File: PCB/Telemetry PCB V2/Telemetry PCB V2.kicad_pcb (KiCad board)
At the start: 4 copper layers, 47 parts, among them IC1 E22-900M22S, J1 USB_C_Receptacle_USB2.0_16P, J2 Batt, J3 Serial Debug Header 1x4, J4 GPS, J5 Conn_01x04_Pin, SW1 SW_MEC_5E, SW2 SW_MEC_5E, U1 AP62200WU, U2 STM32F411CEUx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

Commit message: Corrected spi and uart connections
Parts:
- added C1: 0.1uF, Capacitor_SMD:C_1206_3216Metric_Pad1.33x1.80mm_HandSolder, F.Cu at (208.6, 82.1)
- added D3: WS2812B, LED_SMD:LED_WS2812B_PLCC4_5.0x5.0mm_P3.2mm, F.Cu at (209.6, 77.1)
- C12: value 2.2uF -> 4.7uF
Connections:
- IC1 pad 15: NRST -> TRST
- J4 pad 1: +5V -> +3.3V
- U2 pad 25: RX2 -> TX2
- U2 pad 26: TX2 -> RX2
- U2 pad 29: RX -> unconnected-(U2-PA8-Pad29)
- U2 pad 31: SWDIO -> RX
- U2 pad 32: SWCLK -> unconnected-(U2-PA11-Pad32)
- U2 pad 33: RXEN -> unconnected-(U2-PA12-Pad33)
- U2 pad 34: TXEN -> SWDIO
- U2 pad 37: NSS -> SWCLK
- U2 pad 38: SCK -> unconnected-(U2-PA15-Pad38)
- U2 pad 39: MOSI -> SCK
- U2 pad 41: unconnected-(U2-PB5-Pad41) -> MOSI
- U2 pad 42: BUSY -> unconnected-(U2-PB6-Pad42)
- U2 pad 43: DIO1 -> unconnected-(U2-PB7-Pad43)
- U2 pad 9: VREF+ -> +3.3V
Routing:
- net RXEN: track 44.7 -> 0.00 mm
- net TXEN: track 44.3 -> 0.00 mm
- net BOOT0: track 20.2 -> 0.00 mm
- net SWDIO: track 18.7 -> 0.00 mm
- net SWCLK: track 16.0 -> 0.00 mm
- net DIO1: track 14.9 -> 0.00 mm
- net NSS: track 13.1 -> 0.00 mm
- net BUSY: track 12.9 -> 0.00 mm
- net NRST: track 29.6 -> 16.7 mm, vias 1 -> 0
- net TX2: track 12.6 -> 0.00 mm
- net SCK: track 12.3 -> 0.00 mm
- net MOSI: track 11.5 -> 0.00 mm
- net MISO: track 11.2 -> 0.00 mm
- net RX2: track 10.7 -> 0.00 mm
- removed copper zone on F.Cu, net VREF+

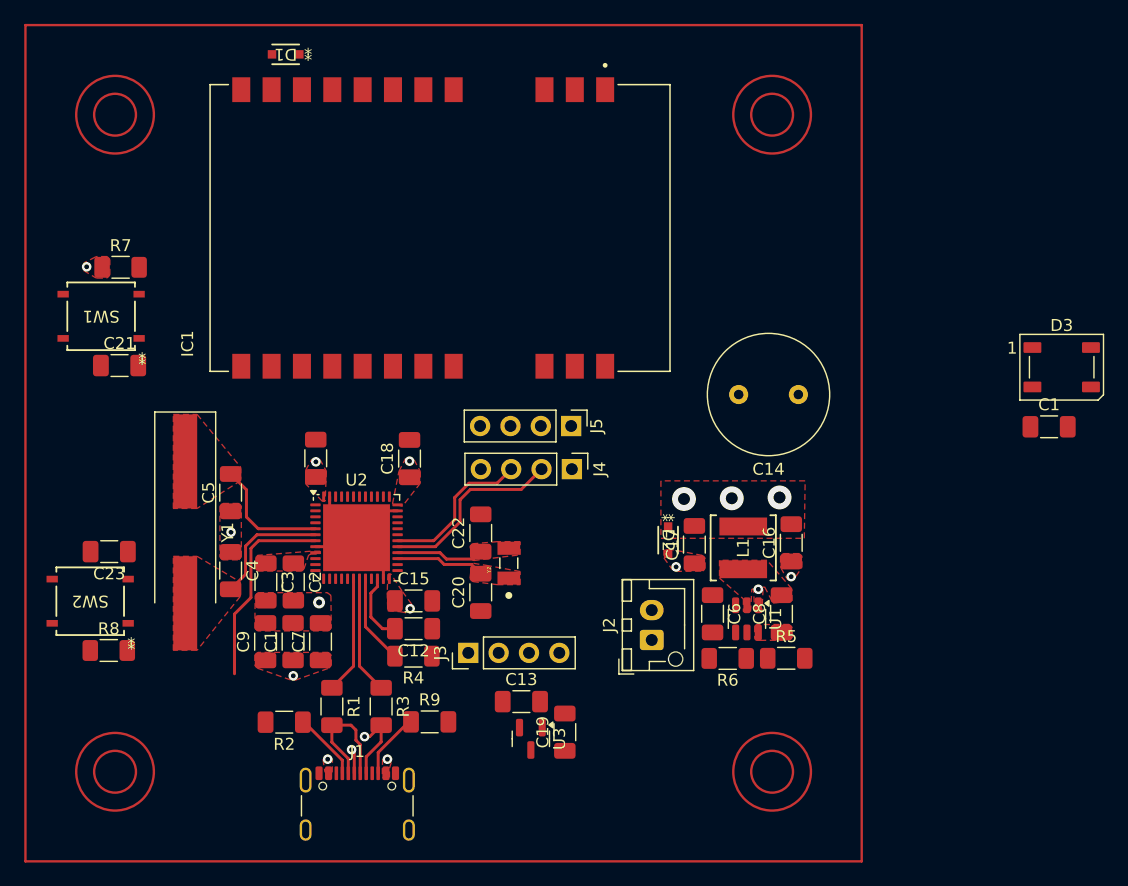
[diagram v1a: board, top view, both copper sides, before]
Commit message: Pins that were wrong are now right
Pins that were wrong are now right and also changed form 1206 capacitors to 0603 capacitors for the load capacitors on the low speed oscillator to reduce size for placement reasons.
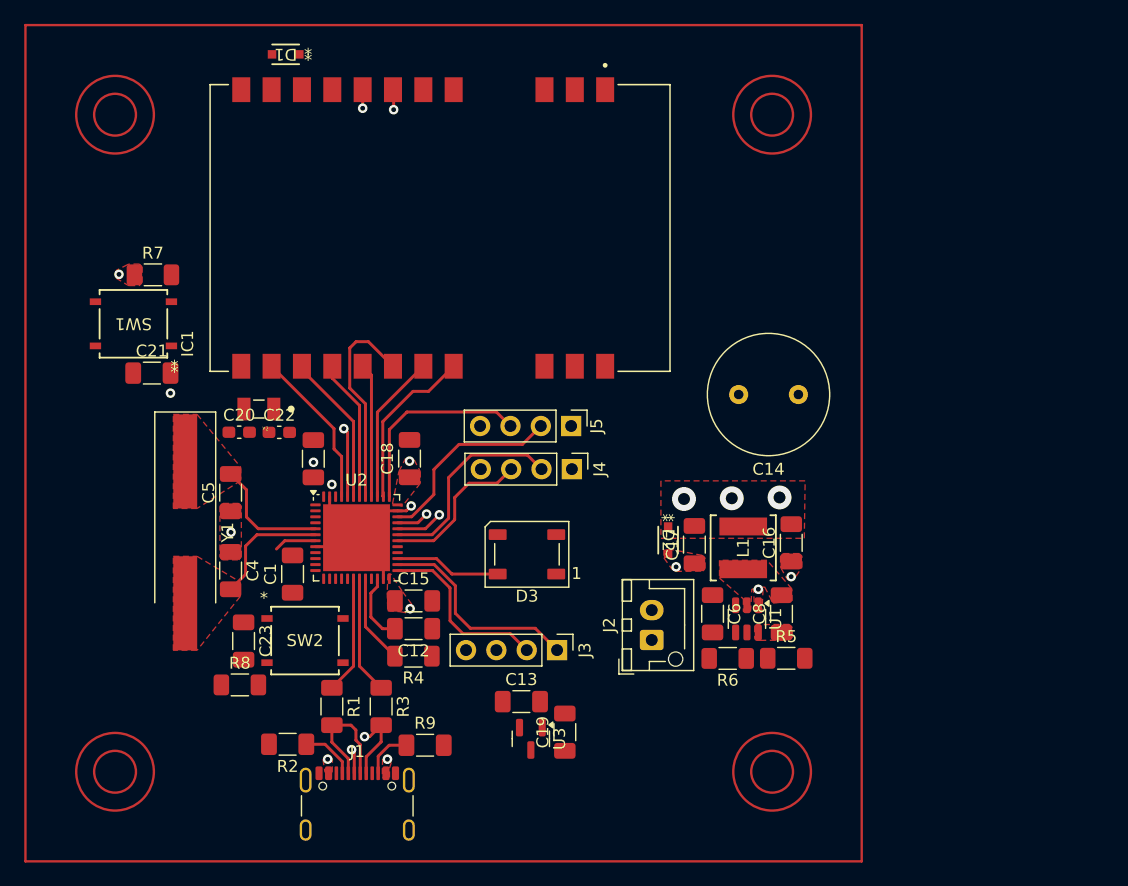
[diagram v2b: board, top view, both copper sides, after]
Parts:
- removed the C1 at (145.3, 100.1)
- removed C2, C7, C9: 0.1uF, Capacitor_SMD:C_1206_3216Metric_Pad1.33x1.80mm_HandSolder
- removed C3: 1uF, Capacitor_SMD:C_1206_3216Metric_Pad1.33x1.80mm_HandSolder
- C20, C22: footprint Capacitor_SMD:C_1206_3216Metric_Pad1.33x1.80mm_HandSolder -> Capacitor_SMD:C_0603_1608Metric_Pad1.08x0.95mm_HandSolder
- moved C1 64.5 mm to (145.3, 94.4), turned to 90 degrees
- moved D3 47.4 mm to (164.9, 92.8), turned to 180 degrees
- moved Y2 24.6 mm to (142.4, 80.6), turned to 180 degrees
- moved C20 24.3 mm to (140.8, 82.5), turned to 0 degrees
- moved C22 18.8 mm to (144.1, 82.5), turned to 0 degrees
- moved SW2 18.3 mm to (146.3, 100.0), turned to 0 degrees
- moved C23 13.5 mm to (141.2, 100.0), turned to -90 degrees
- moved R8 11.3 mm to (140.8, 103.7)
- moved J3 7.43 mm to (167.4, 100.8), turned to -90 degrees
- moved C21 2.78 mm to (133.5, 77.6)
- moved R7 2.78 mm to (133.6, 69.4)
- moved SW1 2.78 mm to (131.9, 73.5)
- moved R9 1.99 mm to (156.4, 108.7)
- moved R2 1.87 mm to (144.8, 108.7)
- moved C11 0.20 mm to (147.0, 84.8)
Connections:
- C20 pad 2: Net-(U2-PB14) -> Net-(U2-PC14)
- C22 pad 1: Net-(U2-PB15) -> Net-(U2-PC15)
- U2 pad 27: Net-(U2-PB14) -> DIN
- U2 pad 28: Net-(U2-PB15) -> unconnected-(U2-PB15-Pad28)
- U2 pad 3: unconnected-(U2-PC14-Pad3) -> Net-(U2-PC14)
- U2 pad 32: unconnected-(U2-PA11-Pad32) -> RXEN
- U2 pad 33: unconnected-(U2-PA12-Pad33) -> TXEN
- U2 pad 38: unconnected-(U2-PA15-Pad38) -> NSS
- U2 pad 4: unconnected-(U2-PC15-Pad4) -> Net-(U2-PC15)
- U2 pad 42: unconnected-(U2-PB6-Pad42) -> TRST
- U2 pad 43: unconnected-(U2-PB7-Pad43) -> BUSY
- U2 pad 45: unconnected-(U2-PB8-Pad45) -> DIO1
- Y2 pad 1: Net-(U2-PB14) -> Net-(U2-PC14)
- Y2 pad 2: Net-(U2-PB15) -> Net-(U2-PC15)
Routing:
- net RXEN: track 0.00 -> 41.1 mm, vias 0 -> 2
- net TXEN: track 0.00 -> 40.5 mm, vias 0 -> 2
- net BOOT0: track 0.00 -> 21.6 mm, vias 0 -> 2
- net MOSI: track 0.00 -> 17.7 mm
- net RX2: track 0.00 -> 17.7 mm
- net SWCLK: track 0.00 -> 16.8 mm
- net SWDIO: track 0.00 -> 16.4 mm
- net TX2: track 0.00 -> 15.2 mm
- net NSS: track 0.00 -> 14.2 mm
- net DIO1: track 0.00 -> 13.3 mm
- net NRST: track 16.7 -> 3.55 mm
- net BUSY: track 0.00 -> 12.7 mm
- net SCK: track 0.00 -> 12.5 mm
- net TRST: track 0.00 -> 11.9 mm
- net MISO: track 0.00 -> 11.2 mm
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- removed copper zone on F.Cu, net Net-(U2-PB14)
- removed copper zone on F.Cu, net Net-(U2-PB15)

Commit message: much progress
Added power planes, edge cuts, and connected many components
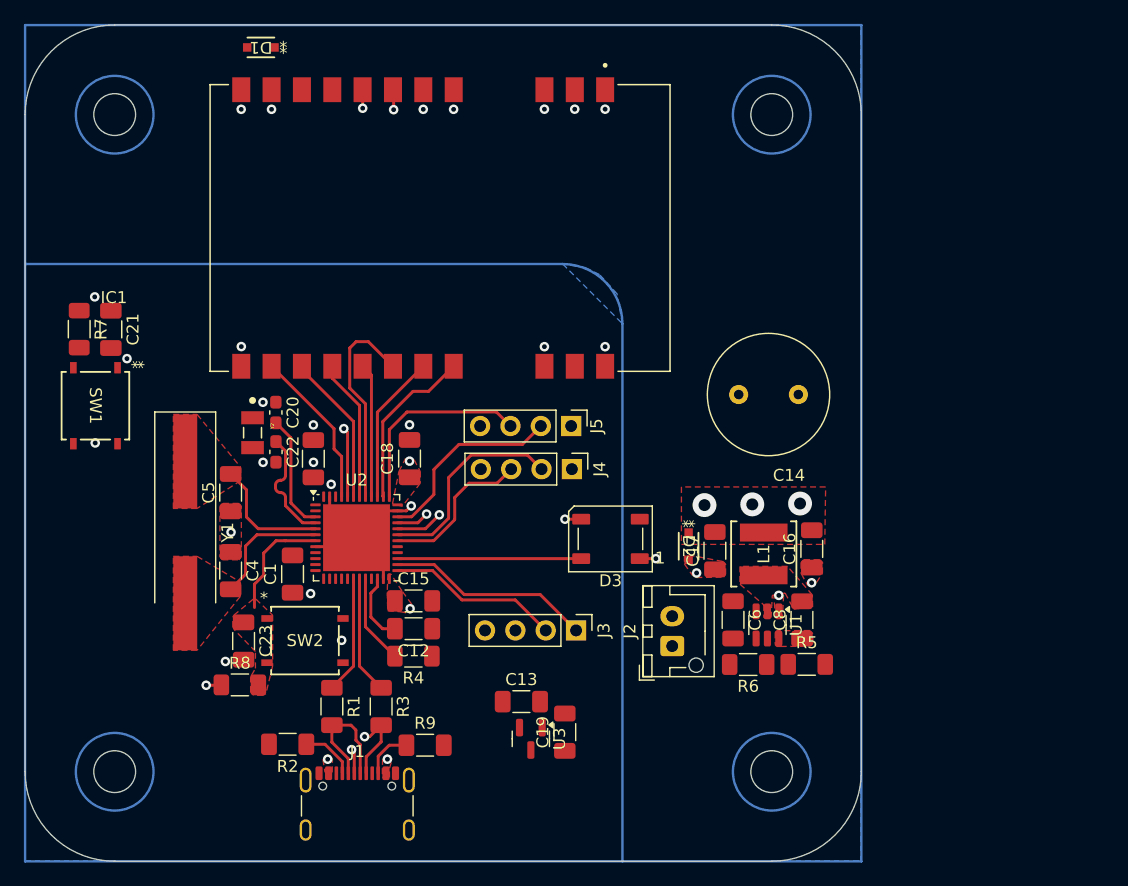
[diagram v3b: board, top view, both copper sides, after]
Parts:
- moved R7 7.66 mm to (127.4, 73.9), turned to -90 degrees
- moved SW1 7.56 mm to (128.8, 80.3), turned to -90 degrees
- moved D3 7.11 mm to (171.9, 91.5)
- moved C21 5.02 mm to (130.0, 73.9), turned to -90 degrees
- moved C20 3.48 mm to (143.9, 80.9), turned to -90 degrees
- moved J3 2.29 mm to (169.0, 99.1)
- moved D1 2.15 mm to (142.6, 50.3)
- moved Y2 2.05 mm to (141.9, 82.6), turned to -90 degrees
- moved C16 1.79 mm to (188.7, 92.3)
- moved C17 1.79 mm to (180.6, 92.4)
- moved C8 1.79 mm to (187.9, 98.2)
- moved J2 1.79 mm to (177.0, 100.4)
- moved R5 1.79 mm to (188.3, 102.0)
- moved C6 1.79 mm to (182.1, 98.2)
- moved D2 1.79 mm to (178.4, 92.1)
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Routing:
- net Net-(U2-PC14): track 0.00 -> 9.77 mm
- net Net-(U2-PC15): track 0.00 -> 9.70 mm
- net DIN: track 8.91 -> 15.4 mm
- net NRST: track 3.55 -> 9.70 mm
- net BOOT0: track 21.6 -> 26.4 mm
- net GND: track 18.2 -> 19.5 mm, vias 6 -> 25
- net +5V: track 0.00 -> 1.35 mm, vias 5 -> 6
- net +3.3V: track 0.00 -> 1.28 mm, vias 3 -> 5
- net TX2: track 15.2 -> 14.5 mm
- net (no net): vias 1 -> 0
- added copper zone on B.Cu, net +3.3V
- added copper zone on B.Cu, net +5V
- added copper zone on In2.Cu, net GND
- added copper zone on F.Cu, net NRST
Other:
- board outline added: 70 x 70 mm

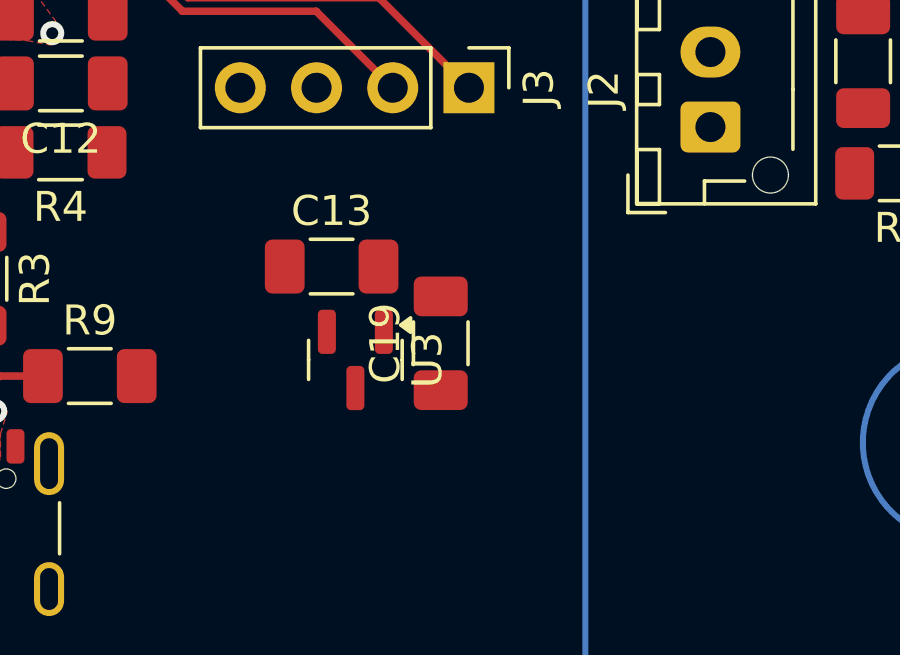
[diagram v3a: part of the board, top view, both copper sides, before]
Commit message: minor placement tweaks
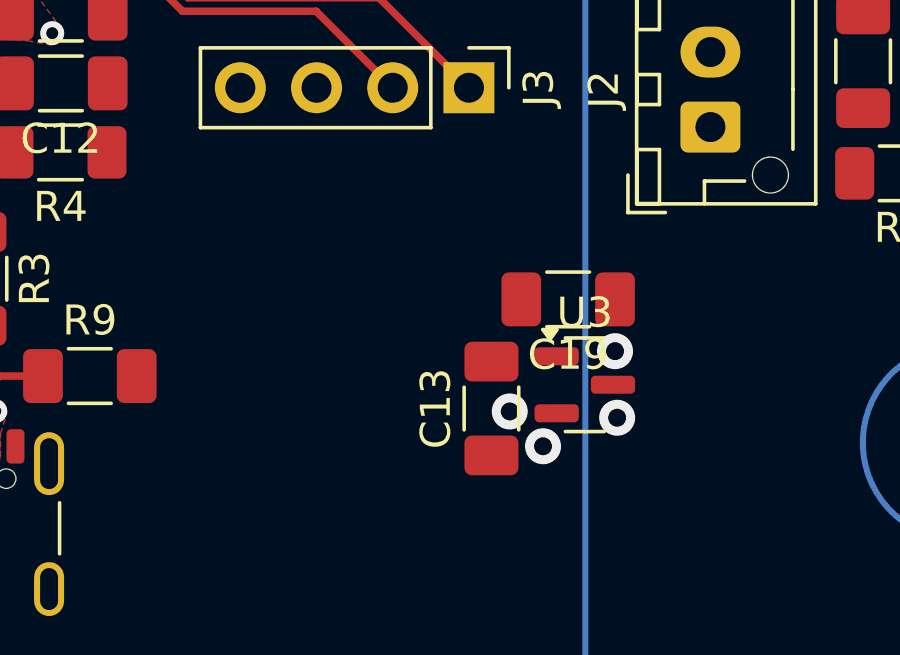
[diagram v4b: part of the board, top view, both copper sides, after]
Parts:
- moved U3 7.69 mm to (172.9, 109.0), turned to 0 degrees
- moved C13 7.13 mm to (169.7, 109.8), turned to 90 degrees
- moved C19 4.49 mm to (172.3, 106.2), turned to 180 degrees
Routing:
- net +5V: vias 6 -> 8
- net +3.3V: vias 5 -> 7

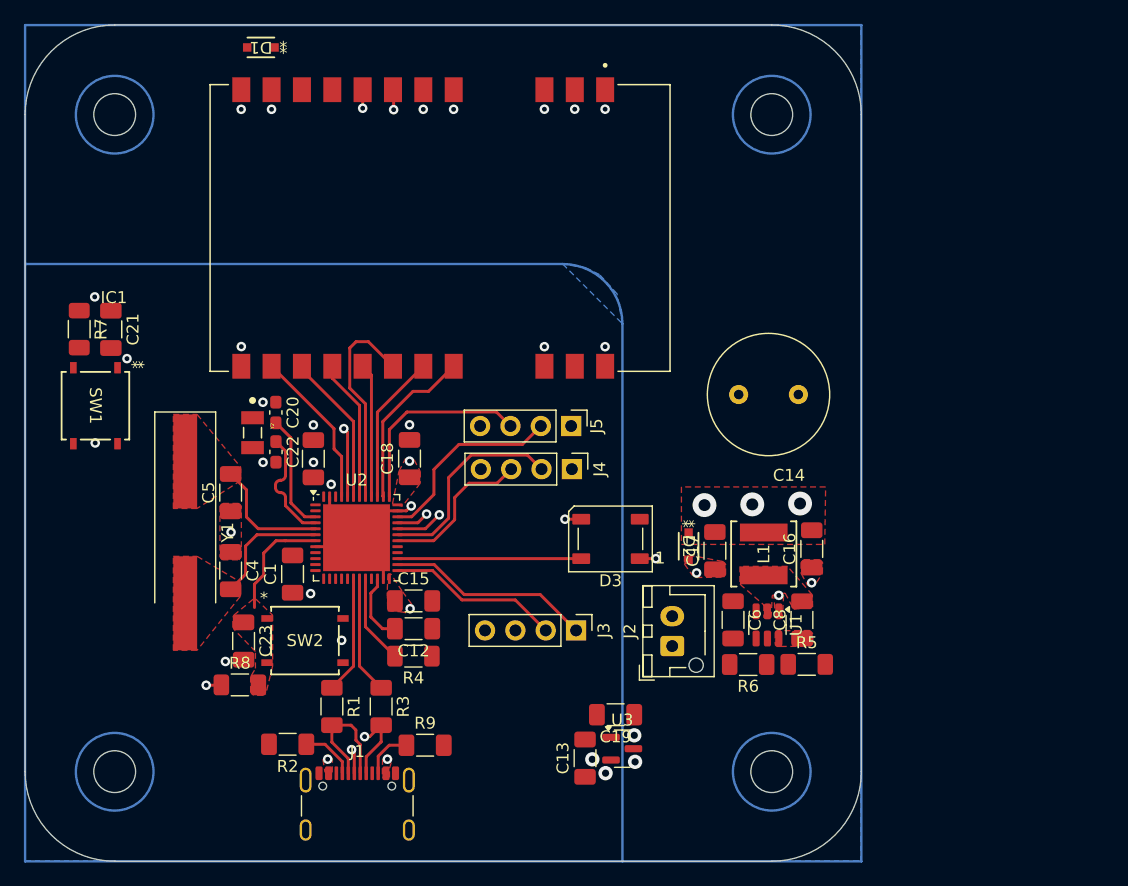
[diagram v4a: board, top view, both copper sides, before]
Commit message: All connections made
All components are now connected all the remains is tweaking a few connections that violate clearances and making the silk screen legible.
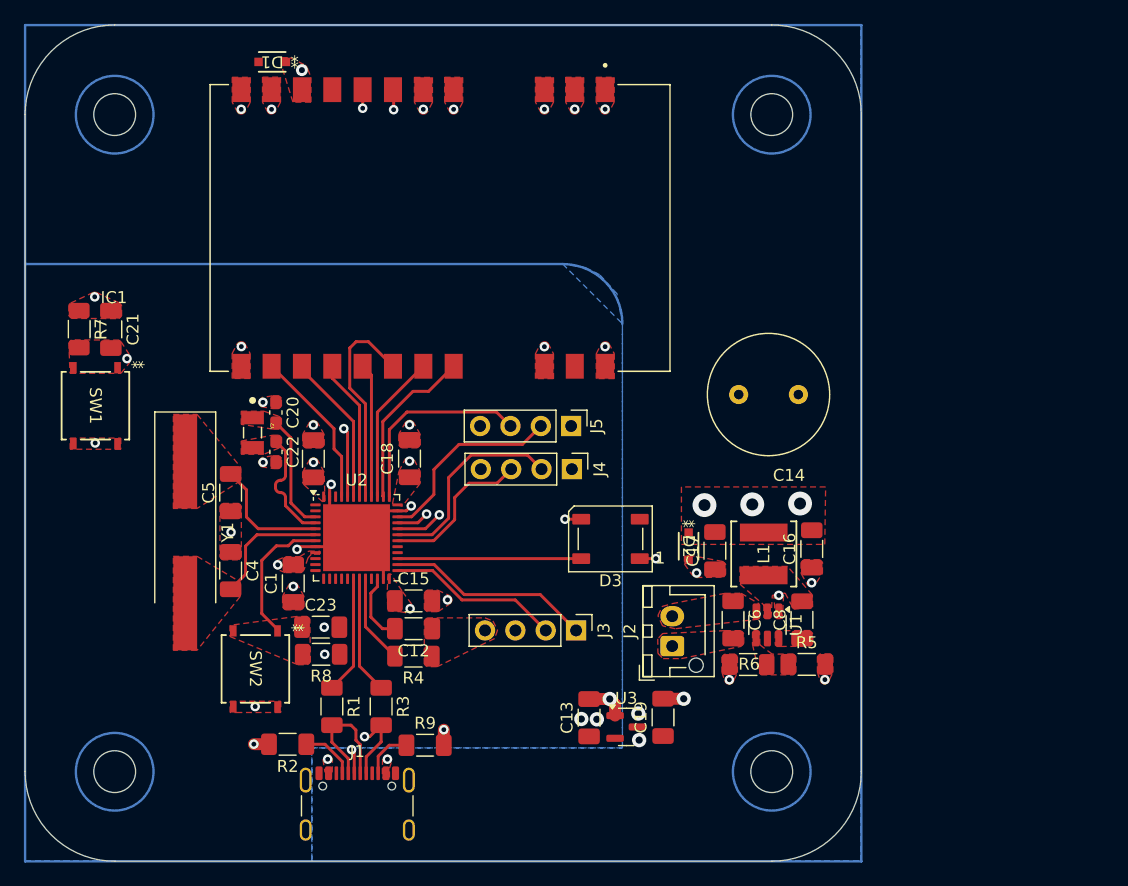
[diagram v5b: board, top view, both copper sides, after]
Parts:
- moved R8 7.27 mm to (147.7, 101.1), turned to 180 degrees
- moved C23 6.55 mm to (147.6, 98.8), turned to 0 degrees
- moved SW2 4.78 mm to (142.2, 102.3), turned to -90 degrees
- moved C19 3.98 mm to (176.3, 106.4), turned to 90 degrees
- moved C13 3.40 mm to (170.1, 106.4)
- moved U3 1.85 mm to (173.2, 107.2)
- moved D1 1.54 mm to (143.6, 51.5)
- moved C1 0.78 mm to (145.3, 95.2)
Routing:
- net GND: track 19.5 -> 29.9 mm, vias 25 -> 32
- net NRST: track 9.70 -> 11.6 mm
- net +3.3V: track 1.28 -> 0.00 mm, vias 7 -> 8
- net +5V: vias 8 -> 10
- added copper zone on F.Cu, net BOOT0
- added copper zone on F.Cu, net Net-(J2-Pin_2)
- added copper zone on F.Cu, net Net-(U1-FB)
- added copper zone on F.Cu, net Net-(U2-PC14)
- added copper zone on F.Cu, net Net-(U2-PC15)
